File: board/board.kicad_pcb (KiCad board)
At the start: 2 copper layers, 21 x 13 mm, 1 part

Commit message: initial
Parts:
- added C1: 2.2uF, Capacitor_SMD:C_1206_3216Metric, F.Cu at (144.5, 95.5)
- added C2: 2.2uF, Capacitor_SMD:C_1206_3216Metric, F.Cu at (148.0, 97.7)
- added C3: 100nF, Capacitor_SMD:C_0603_1608Metric, F.Cu at (152.3, 94.6)
- added C4: d.n.p, Capacitor_SMD:C_0603_1608Metric, F.Cu at (145.2, 91.6)
- added C5: 10uF, Capacitor_SMD:C_0603_1608Metric, F.Cu at (148.8, 101.1)
- added C6: 10uF, Capacitor_SMD:C_0603_1608Metric, F.Cu at (148.8, 99.6)
- added J1: Conn_01x03_Male, Connector_PinHeader_2.54mm:PinHeader_1x03_P2.54mm_Vertical, F.Cu at (141.5, 93.5)
- added J2: 003_power, on_edge:on_edge_2x05_host, F.Cu at (161.0, 96.5)
- added L1: 8.2uH, Inductor_SMD:L_1008_2520Metric, F.Cu at (151.7, 98.5)
- added R1: 69.8k, Resistor_SMD:R_0603_1608Metric, F.Cu at (146.7, 91.6)
- added R2: 22.1k, Resistor_SMD:R_0603_1608Metric, F.Cu at (149.0, 91.6)
- added U1: AP63200WU, Package_TO_SOT_SMD:TSOT-23-6, F.Cu at (149.8, 94.4)
- LOGO1: moved to B.Cu
- moved LOGO1 2.28 mm to (152.2, 98.4), turned to 180 degrees
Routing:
- net GND: track 0.00 -> 33.5 mm, vias 0 -> 26
- net /step_down/out: track 0.00 -> 21.9 mm, vias 0 -> 3
- net /step_down/in: track 0.00 -> 13.9 mm, vias 0 -> 2
- net /step_down/SW: track 0.00 -> 8.89 mm
- net /step_down/EN: track 0.00 -> 8.61 mm, vias 0 -> 1
- net /step_down/FB: track 0.00 -> 5.28 mm
- net Net-(C3-Pad2): track 0.00 -> 2.02 mm
- added copper zone on B.Cu, net GND
- added copper zone on F.Cu, net GND
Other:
- outline, holes or cut-outs redrawn
- board text added: "osf.003"
- board text added: "osf.b113.v1.0"

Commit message: fixed incorrect part number
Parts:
- U1: value AP63200WU -> AP64060
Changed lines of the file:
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@@
       (effects (font (size 1 1) (thickness 0.15)))
     )
-    (fp_text value "AP63200WU" (at 0 2.4 90) (layer "F.Fab")
+    (fp_text value "AP64060" (at 0 2.4 90) (layer "F.Fab")
       (effects (font (size 1 1) (thickness 0.15)))
     )

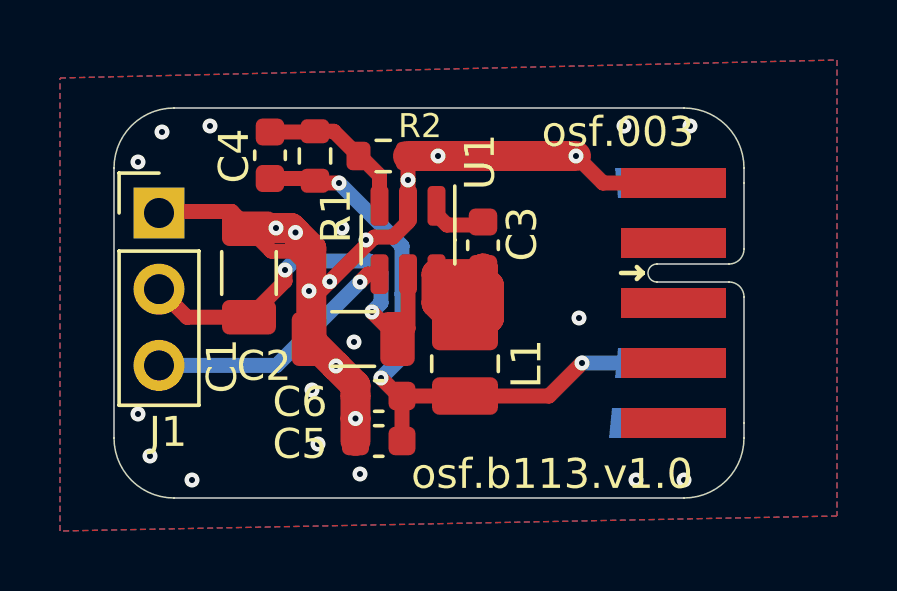
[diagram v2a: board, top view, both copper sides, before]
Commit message: used lower dc resistance inductor
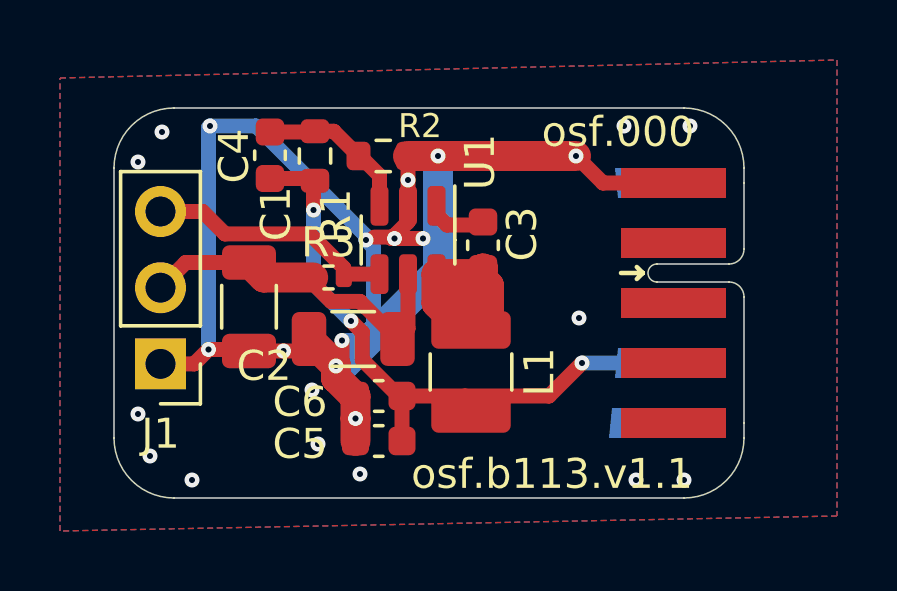
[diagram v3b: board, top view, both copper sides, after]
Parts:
- added R3: 0R, Resistor_SMD:R_0402_1005Metric, F.Cu at (147.2, 95.7)
- L1: value 8.2uH -> 10uH; footprint Inductor_SMD:L_1008_2520Metric -> Inductor_SMD:L_1210_3225Metric
- moved J1 5.03 mm to (141.6, 98.5), turned to 180 degrees
- moved C1 1.12 mm to (144.5, 96.6), turned to -90 degrees
- moved L1 0.34 mm to (151.9, 98.8)
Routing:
- net GND: track 33.5 -> 51.3 mm, vias 26 -> 25
- net /step_down/in: track 13.9 -> 11.7 mm, vias 2 -> 0
- net /step_down/out: track 21.9 -> 21.0 mm
- net /step_down/EN: track 8.61 -> 8.45 mm, vias 1 -> 0
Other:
- board text added: "osf.000"
- board text added: "osf.b113.v1.1"
- board text removed: "osf.003"
- board text removed: "osf.b113.v1.0"
